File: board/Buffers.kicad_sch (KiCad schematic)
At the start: 13 parts, among them IC9 LF353P, U58 74F541, U59 74F245, U60 74F541, U61 74F125

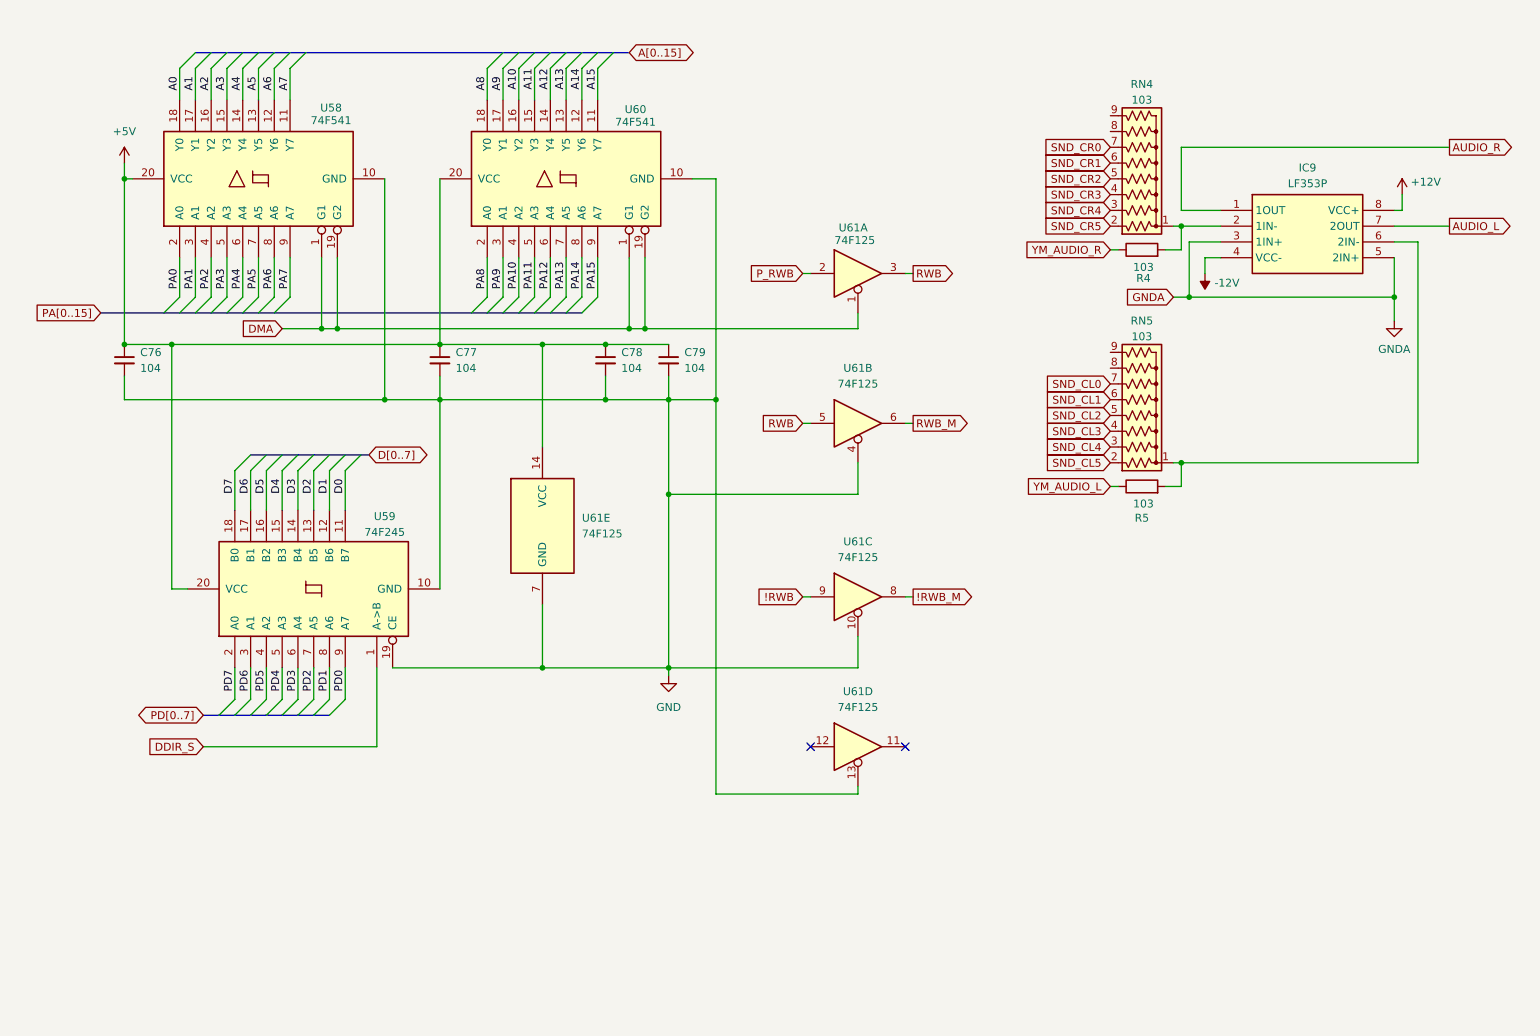
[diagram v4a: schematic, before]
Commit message: 1.7C: Logic corrections and placement tweaks
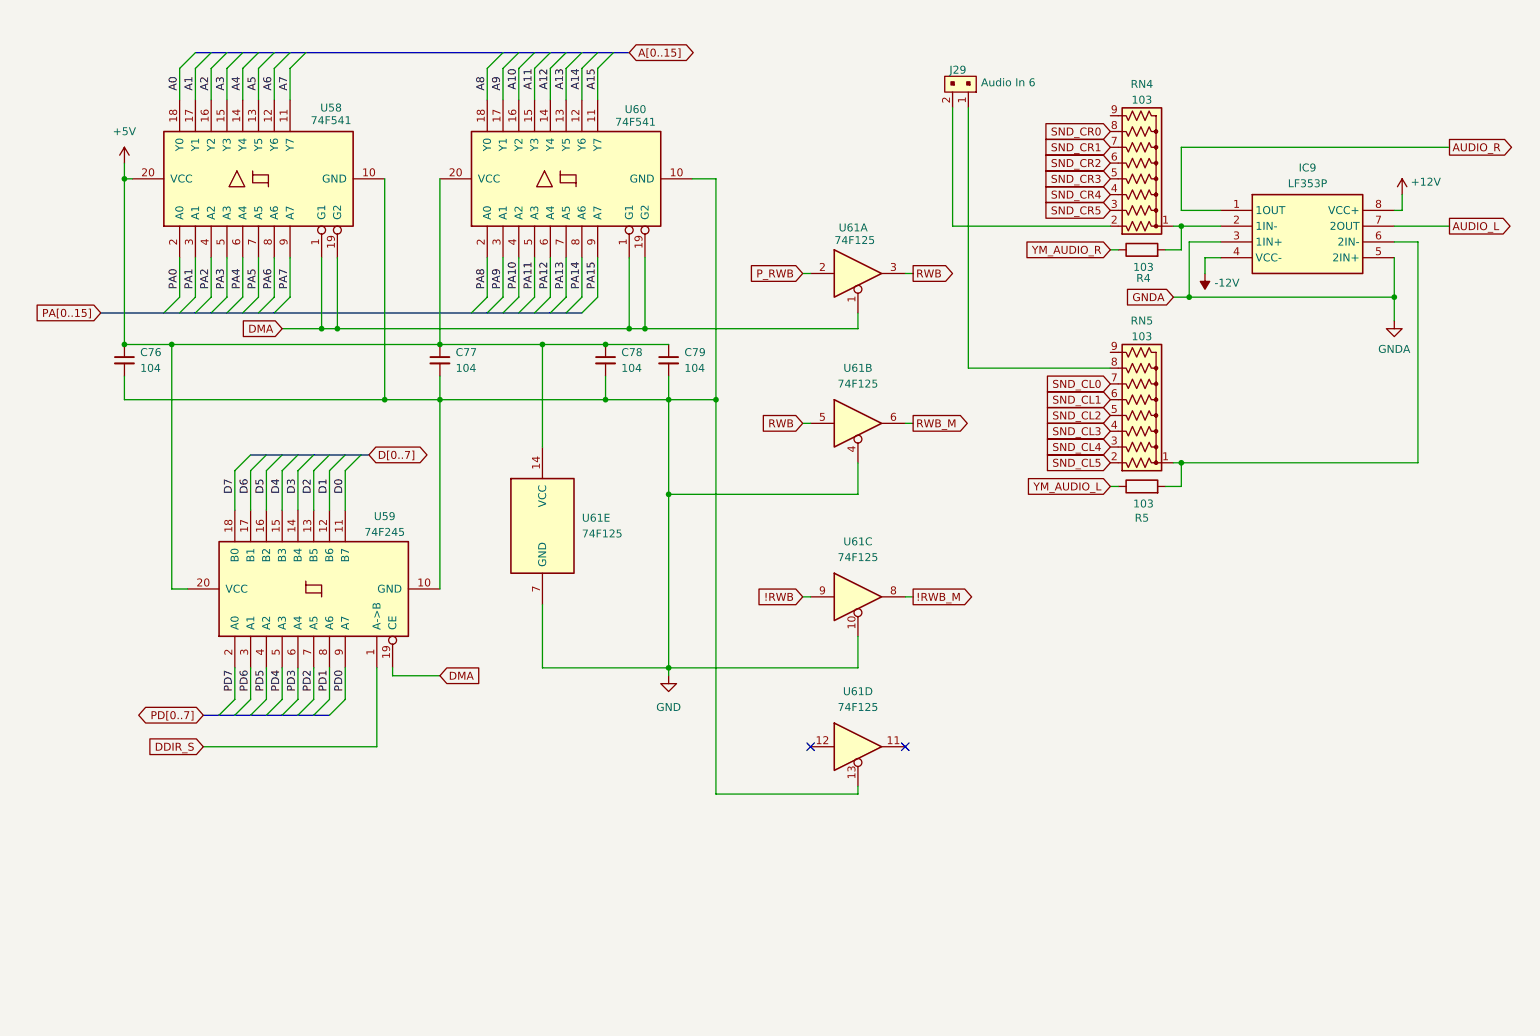
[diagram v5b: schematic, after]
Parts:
- added J29: Audio In 6, Connector_PinHeader_2.54mm:PinHeader_2x01_P2.54mm_Vertical, symbol dk_Rectangular-Connectors-Headers-Male-Pins:22-23-2021
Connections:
- net DMA: now also U59.19 (CE)
- net GND: no longer U59.19 (CE)
- net SND_CR0: now also RN4.8 (R7); no longer RN4.7 (R6)
- net SND_CR1: now also RN4.7 (R6); no longer RN4.6 (R5)
- net SND_CR2: now also RN4.6 (R5); no longer RN4.5 (R4)
- net SND_CR3: now also RN4.5 (R4); no longer RN4.4 (R3)
- net SND_CR4: now also RN4.4 (R3); no longer RN4.3 (R2)
- net SND_CR5: now also RN4.3 (R2); no longer RN4.2 (R1)
- net at RN5.8 (R7): now also J29.1
- new net: J29.2, RN4.2 (R1)

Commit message: V1.8C production board
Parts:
- removed IC9: LF353P, Package_DIP:DIP-8_W7.62mm_Socket_LongPads, symbol LF353:LF353P
- removed J29: Audio In 6, Connector_PinHeader_2.54mm:PinHeader_2x01_P2.54mm_Vertical, symbol dk_Rectangular-Connectors-Headers-Male-Pins:22-23-2021
- removed R4, R5: 103, Resistor_THT:R_Axial_DIN0204_L3.6mm_D1.6mm_P5.08mm_Horizontal, symbol Device:R
- removed RN4, RN5: 103, Resistor_THT:R_Array_SIP9, symbol Device:R_Network08_US
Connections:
- net +5V: now also U61.12, U61.13
- net D0: now also U59.18 (B0); no longer U59.11 (B7)
- net D1: now also U59.17 (B1); no longer U59.12 (B6)
- net D2: now also U59.16 (B2); no longer U59.13 (B5)
- net D3: now also U59.15 (B3); no longer U59.14 (B4)
- net D4: now also U59.14 (B4); no longer U59.15 (B3)
- net D5: now also U59.13 (B5); no longer U59.16 (B2)
- net D6: now also U59.12 (B6); no longer U59.17 (B1)
- net D7: now also U59.11 (B7); no longer U59.18 (B0)
- net GND: no longer U61.13
- net PD0: now also U59.2 (A0); no longer U59.9 (A7)
- net PD1: now also U59.3 (A1); no longer U59.8 (A6)
- net PD2: now also U59.4 (A2); no longer U59.7 (A5)
- net PD3: now also U59.5 (A3); no longer U59.6 (A4)
- net PD4: now also U59.6 (A4); no longer U59.5 (A3)
- net PD5: now also U59.7 (A5); no longer U59.4 (A2)
- net PD6: now also U59.8 (A6); no longer U59.3 (A1)
- net PD7: now also U59.9 (A7); no longer U59.2 (A0)
- no-connect marks 2 -> 1
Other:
- moved on the sheet: U61A, U61B, U61C, U61D, U61E
